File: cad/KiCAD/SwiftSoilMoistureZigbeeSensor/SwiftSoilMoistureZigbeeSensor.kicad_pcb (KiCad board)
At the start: 2 copper layers, 80 x 22.9 mm, 12 parts, among them J1 Probe, J3 ARM SWD, Q1 BSS84, SW1 Factory Reset, U1 TPS61221DCK, U2 E73-2G4M08S1C

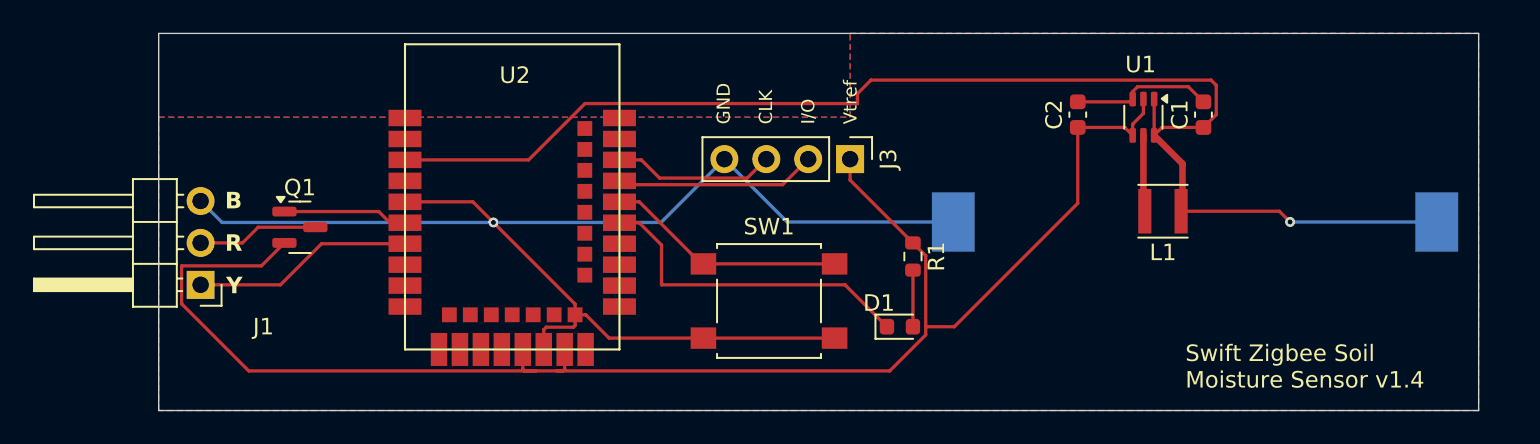
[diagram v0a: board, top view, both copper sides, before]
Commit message: Changed TPS61221 to TPS61097
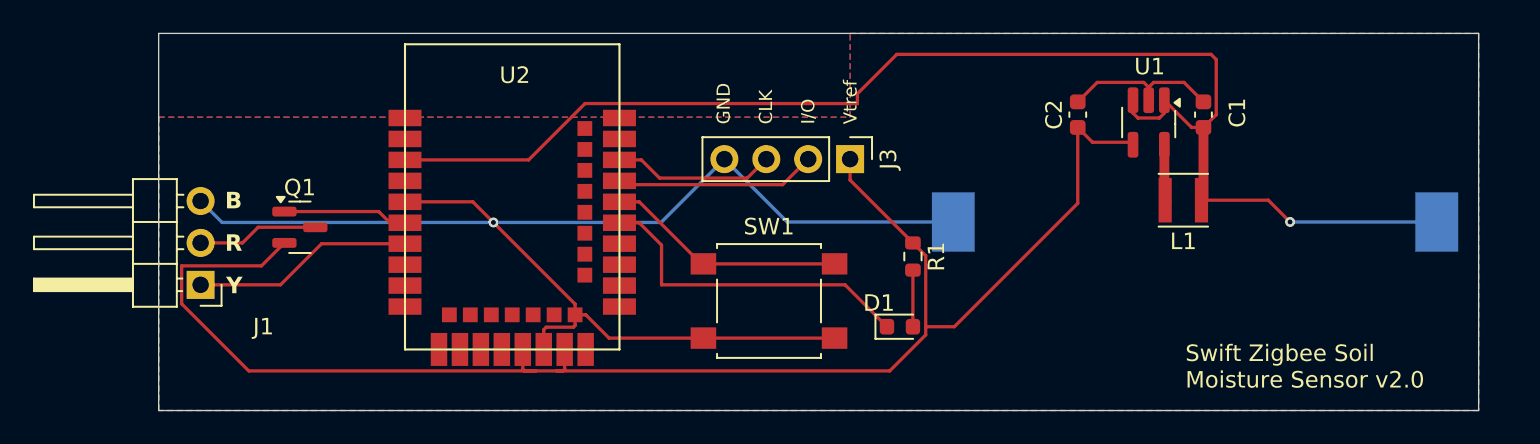
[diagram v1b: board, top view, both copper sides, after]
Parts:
- U1: value TPS61221DCK -> TPS61097A-33DBVR; footprint Package_TO_SOT_SMD:Texas_R-PDSO-G6 -> Package_TO_SOT_SMD:SOT-23-5_HandSoldering
- moved L1 1.41 mm to (130.7, 68.5)
- moved U1 0.45 mm to (128.6, 63.8)
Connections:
- U1 pad 2: +3.3V -> GND
- U1 pad 3: GND -> Net-(BT1-+)
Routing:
- net +3.3V: track 96.0 -> 93.7 mm
- net Net-(BT1-+): track 80.9 -> 82.8 mm
- net GND: track 91.7 -> 92.7 mm
- net Net-(U1-L): track 4.60 -> 3.86 mm
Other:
- board text added: "Swift Zigbee Soil Moisture Sensor v2.0"
- board text removed: "Swift Zigbee Soil Moisture Sensor v1.4"
